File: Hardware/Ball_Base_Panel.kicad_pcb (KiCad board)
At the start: 4 copper layers, 20 x 128.5 mm, 12 parts

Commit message: Preparation of Gerbers for manufacturing
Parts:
- moved G*** 4.30 mm to (80.3, 143.3)
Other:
- outline, holes or cut-outs redrawn
- copper layers 4 -> 2
- board text added: "JLCJLCJLCJLC"
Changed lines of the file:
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@@
 (kicad_pcb (version 20211014) (generator pcbnew)
   (general
-    (thickness 1.5927)
+    (thickness 0.2927)
   )
   (paper "A4")
   (layers
     (0 "F.Cu" signal)
-    (1 "In1.Cu" signal)
-    (2 "In2.Cu" signal)
     (31 "B.Cu" signal)
     (32 "B.Adhes" user "B.Adhesive")
@@
     (40 "Dwgs.User" user "User.Drawings")
     (41 "Cmts.User" user "User.Comments")
-    (42 "Eco1.User" user "User.Eco1")
-    (43 "Eco2.User" user "User.Eco2")
     (44 "Edge.Cuts" user)
     (45 "Margin" user)
@@
     (48 "B.Fab" user)
     (49 "F.Fab" user)
-    (50 "User.1" user)
-    (51 "User.2" user)
-    (52 "User.3" user)
-    (53 "User.4" user)
-    (54 "User.5" user)
-    (55 "User.6" user)
-    (56 "User.7" user)
-    (57 "User.8" user)
-    (58 "User.9" user)
   )
   (setup
@@
       (layer "F.Cu" (type "copper") (thickness 0.035))
       (layer "dielectric 1" (type "core") (thickness 0.2) (material "FR4") (epsilon_r 4.5) (loss_tangent 0.02))
-      (layer "In1.Cu" (type "copper") (thickness 0.0175))
-      (layer "dielectric 2" (type "prepreg") (thickness 1.065) (material "FR4") (epsilon_r 4.5) (loss_tangent 0.02))
-      (layer "In2.Cu" (type "copper") (thickness 0.0175))
-      (layer "dielectric 3" (type "core") (thickness 0.2) (material "FR4") (epsilon_r 4.5) (loss_tangent 0.02))
       (layer "B.Cu" (type "copper") (thickness 0.035))
       (layer "B.Mask" (type "Bottom Solder Mask") (color "Black") (thickness 0.01))
@@
       (outputformat 1)
       (mirror false)
-      (drillshape 1)
+      (drillshape 0)
       (scaleselection 1)
-      (outputdirectory "")
+      (outputdirectory "Gerbers/Ball_Base_Panel/")
     )
   )
@@
   )
   (footprint "Custom_Footprints:bluetooth" (layer "F.Cu")
-    (at 84.6 143.3)
+    (at 80.3 143.3)
     (attr board_only exclude_from_pos_files exclude_from_bom)
     (fp_text reference "G***" (at 0 0) (layer "F.SilkS") hide
@@
       (polygon
         (pts
-          (xy 87.054377 139.745039)
-          (xy 87.3 140.7)
-          (xy 87.3 146.1)
-          (xy 87 146.8)
-          (xy 86.2 147.3)
-          (xy 82.95 147.3)
-          (xy 82.225 146.825)
-          (xy 81.9 146.25)
-          (xy 81.9 140.45)
-          (xy 82.25 139.7)
-          (xy 83.05 139.3)
-          (xy 86.15 139.3)
+          (xy 82.754377 139.745039)
+          (xy 83 140.7)
+          (xy 83 146.1)
+          (xy 82.7 146.8)
+          (xy 81.9 147.3)
+          (xy 78.65 147.3)
+          (xy 77.925 146.825)
+          (xy 77.6 146.25)
+          (xy 77.6 140.45)
+          (xy 77.95 139.7)
+          (xy 78.75 139.3)
+          (xy 81.85 139.3)
         )
       )
@@
   (gr_line (start 90.3 97) (end 70.3 97) (layer "Dwgs.User") (width 0.15))
   (gr_rect (start 70.3 39.5) (end 90.3 168) (layer "Edge.Cuts") (width 0.1) (fill none))
-  (gr_line (start 73.203553 138.453553) (end 73.203553 148.246447) (layer "Edge.Cuts") (width 0.1))
-  (gr_arc (start 77.496447 148.246447) (mid 77.35 148.6) (end 76.996447 148.746447) (layer "Edge.Cuts") (width 0.1))
-  (gr_arc (start 73.703553 148.746447) (mid 73.35 148.6) (end 73.203553 148.246447) (layer "Edge.Cuts") (width 0.1))
-  (gr_line (start 77.496447 148.246447) (end 77.496447 138.453553) (layer "Edge.Cuts") (width 0.1))
-  (gr_line (start 73.703553 137.953553) (end 76.996447 137.953553) (layer "Edge.Cuts") (width 0.1))
-  (gr_line (start 73.703553 148.746447) (end 76.996447 148.746447) (layer "Edge.Cuts") (width 0.1))
-  (gr_arc (start 76.996447 137.953553) (mid 77.35 138.1) (end 77.496447 138.453553) (layer "Edge.Cuts") (width 0.1))
-  (gr_arc (start 73.203553 138.453553) (mid 73.35 138.1) (end 73.703553 137.953553) (layer "Edge.Cuts") (width 0.1))
   (gr_rect (start 73.2 148.5) (end 77.5 138.2) (layer "F.Fab") (width 0.1) (fill none))
+  (gr_text "JLCJLCJLCJLC" (at 80.4 156.9) (layer "B.SilkS")
+    (effects (font (size 1 1) (thickness 0.15)) (justify mirror))
+  )
   (gr_text "Ball Panel v1.0" (at 80.3 47.4) (layer "B.SilkS")
     (effects (font (size 1 1) (thickness 0.15)) (justify mirror))

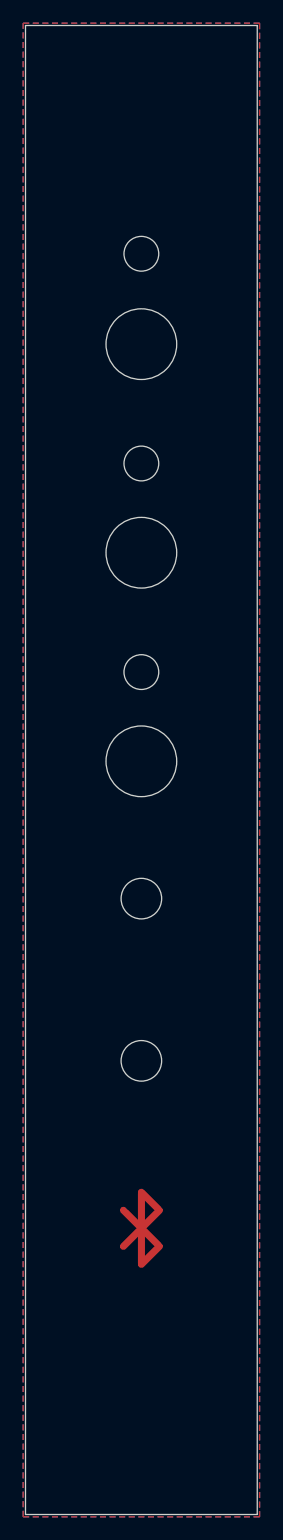
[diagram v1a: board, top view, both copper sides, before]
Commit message: Updated panel to reduce copper pour and solder mask
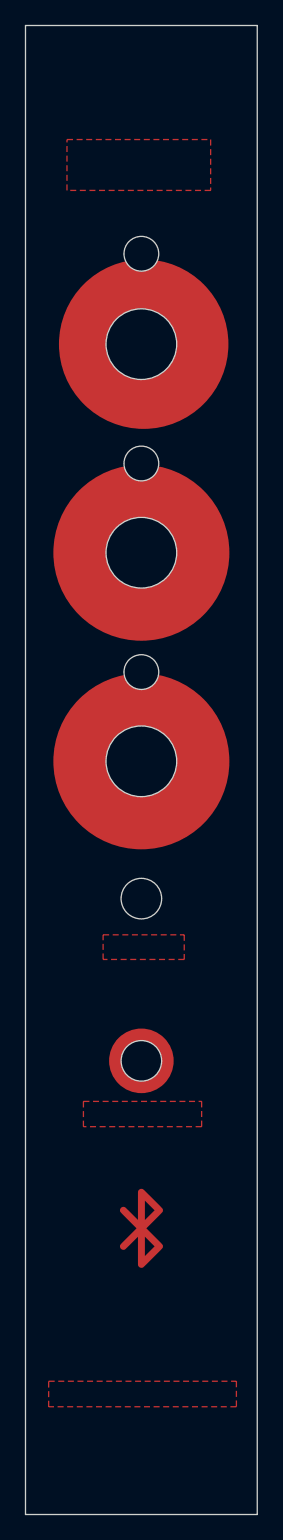
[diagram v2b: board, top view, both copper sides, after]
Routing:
- removed copper zone on B.Cu, net (none)
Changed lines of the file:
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@@
     (fp_circle (center 0 0) (end 4.3 0) (layer "F.CrtYd") (width 0.05) (fill none))
     (pad "" np_thru_hole circle locked (at 0 0) (size 6.1 6.1) (drill 6.1) (layers *.Cu *.Mask "F.SilkS"))
-    (model "D:/kiCad/Custom_Footprints.pretty/3dmodels/PJ302M_Hex_nut.step"
-      (offset (xyz -5.05 -0 -1.5))
+    (model "${CUSTOM_3D}/PJ302M_Hex_nut.step"
+      (offset (xyz -5.05 0 -1.5))
       (scale (xyz 1 1 1))
       (rotate (xyz 90 0 90))
@@
     (fp_circle (center 0 0) (end 4.3 0) (layer "F.CrtYd") (width 0.05) (fill none))
     (pad "" np_thru_hole circle locked (at 0 0) (size 6.1 6.1) (drill 6.1) (layers *.Cu *.Mask "F.SilkS"))
-    (model "D:/kiCad/Custom_Footprints.pretty/3dmodels/PJ302M_Hex_nut.step"
-      (offset (xyz -5.05 -0 -1.5))
+    (model "${CUSTOM_3D}/PJ302M_Hex_nut.step"
+      (offset (xyz -5.05 0 -1.5))
       (scale (xyz 1 1 1))
       (rotate (xyz 90 0 90))
@@
     (fp_circle (center 0 0) (end 4.3 0) (layer "F.CrtYd") (width 0.05) (fill none))
     (pad "" np_thru_hole circle locked (at 0 0) (size 6.1 6.1) (drill 6.1) (layers *.Cu *.Mask "F.SilkS"))
-    (model "D:/kiCad/Custom_Footprints.pretty/3dmodels/PJ302M_Hex_nut.step"
-      (offset (xyz -5.05 -0 -1.5))
+    (model "${CUSTOM_3D}/PJ302M_Hex_nut.step"
+      (offset (xyz -5.05 0 -1.5))
       (scale (xyz 1 1 1))
       (rotate (xyz 90 0 90))
@@
     )
   )
+  (gr_circle (center 80.5 67) (end 87.712489 67) (layer "F.Cu") (width 0.2) (fill solid))
+  (gr_circle (center 80.3 128.85) (end 82.987006 128.85) (layer "F.Cu") (width 0.2) (fill solid))
+  (gr_circle (center 80.3 103) (end 87.795332 103) (layer "F.Cu") (width 0.2) (fill solid))
+  (gr_circle (center 80.3 85) (end 87.795332 85) (layer "F.Cu") (width 0.2) (fill solid))
+  (gr_rect (start 90.7 156.5) (end 69.9 55) (layer "B.Mask") (width 0.15) (fill solid))
   (gr_circle (center 80.3 66.980309) (end 87.419691 66.980309) (layer "F.Mask") (width 0.4) (fill none))
   (gr_circle (center 80.3 85) (end 87.419691 85) (layer "F.Mask") (width 0.4) (fill none))
@@
   (gr_line (start 90.2 113.1) (end 70.3 113.1) (layer "Dwgs.User") (width 0.15))
   (gr_rect (start 75 56) (end 73.4 156) (layer "Dwgs.User") (width 0.15) (fill none))
-  (gr_line (start 122.15 138.4) (end 70.3 138.4) (layer "Dwgs.User") (width 0.15))
+  (gr_line (start 90.3 138.4) (end 70.3 138.4) (layer "Dwgs.User") (width 0.15))
   (gr_line (start 90.3 82) (end 70.3 82) (layer "Dwgs.User") (width 0.15))
   (gr_line (start 90.3 127.1) (end 70.3 127.1) (layer "Dwgs.User") (width 0.15))
@@
   (gr_rect (start 70.3 39.5) (end 90.3 168) (layer "Edge.Cuts") (width 0.1) (fill none))
   (gr_rect (start 73.2 148.5) (end 77.5 138.2) (layer "F.Fab") (width 0.1) (fill none))
-  (gr_text "JLCJLCJLCJLC" (at 80.4 156.9) (layer "B.SilkS")
+  (gr_text "JLCJLCJLCJLC" (at 80.4 159.5) (layer "B.SilkS")
     (effects (font (size 1 1) (thickness 0.15)) (justify mirror))
   )
@@
     (effects (font (size 1.7 1.7) (thickness 0.25)))
   )
-  (gr_text "Mountjoy Modular" (at 80.3 152.85) (layer "F.Mask")
+  (gr_text "Mountjoy Modular" (at 80.3 157.5) (layer "F.Mask")
     (effects (font (size 1.2 1.2) (thickness 0.2)))
   )
@@
     (effects (font (size 1 1) (thickness 0.15)))
   )
-  (zone (net 0) (net_name "") (layers F&B.Cu) (hatch edge 0.508)
+  (zone (net 0) (net_name "") (layer "F.Cu") (hatch edge 0.508)
     (connect_pads (clearance 0.508))
     (min_thickness 0.254) (filled_areas_thickness no)
@@
     (polygon
       (pts
-        (xy 90.5 168.2)
-        (xy 70.1 168.2)
-        (xy 70.1 39.3)
-        (xy 90.5 39.3)
+        (xy 84 120.1)
+        (xy 77 120.1)
+        (xy 77.000001 117.973222)
+        (xy 84.000001 117.973222)
       )
     )
   )
-  (zone (net 0) (net_name "") (layers F&B.Cu) (hatch edge 0.508)
-    (connect_pads (clearance 0))
-    (min_thickness 0.254)
-    (keepout (tracks allowed) (vias allowed) (pads allowed ) (copperpour not_allowed) (footprints allowed))
-    (fill (thermal_gap 0.508) (thermal_bridge_width 0.508))
+  (zone (net 0) (net_name "") (layer "F.Cu") (hatch edge 0.508)
+    (connect_pads (clearance 0.508))
+    (min_thickness 0.254) (filled_areas_thickness no)
+    (fill yes (thermal_gap 0.508) (thermal_bridge_width 0.508))
     (polygon
       (pts
-        (xy 90.3 148.8)
-        (xy 88.9 150.2)
-        (xy 71.7 150.2)
-        (xy 70.3 148.8)
-        (xy 70.3 137.9)
-        (xy 71.7 136.5)
-        (xy 88.9 136.5)
-        (xy 90.3 137.9)
+        (xy 88.5 158.7)
+        (xy 72.3 158.7)
+        (xy 72.3 156.5)
+        (xy 88.5 156.5)
       )
     )
+  )
+  (zone (net 0) (net_name "") (layer "F.Cu") (hatch edge 0.508)
+    (connect_pads (clearance 0.508))
+    (min_thickness 0.254) (filled_areas_thickness no)
+    (fill yes (thermal_gap 0.508) (thermal_bridge_width 0.508))
+    (polygon
+      (pts
+        (xy 86.277751 53.732931)
+        (xy 73.881402 53.73293)
+        (xy 73.881402 49.342131)
+        (xy 86.277751 49.342132)
+      )
+    )
+  )
+  (zone (net 0) (net_name "") (layer "F.Cu") (hatch edge 0.508)
+    (connect_pads (clearance 0.508))
+    (min_thickness 0.254) (filled_areas_thickness no)
+    (fill yes (thermal_gap 0.508) (thermal_bridge_width 0.508))
+    (polygon
+      (pts
+        (xy 85.5 134.529748)
+        (xy 75.3 134.529748)
+        (xy 75.300001 132.34963)
+        (xy 85.500001 132.34963)
+      )
+    )
